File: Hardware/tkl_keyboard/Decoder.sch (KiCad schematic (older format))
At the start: 8 parts, among them U7 CD74HC238, U8 CD74HC238

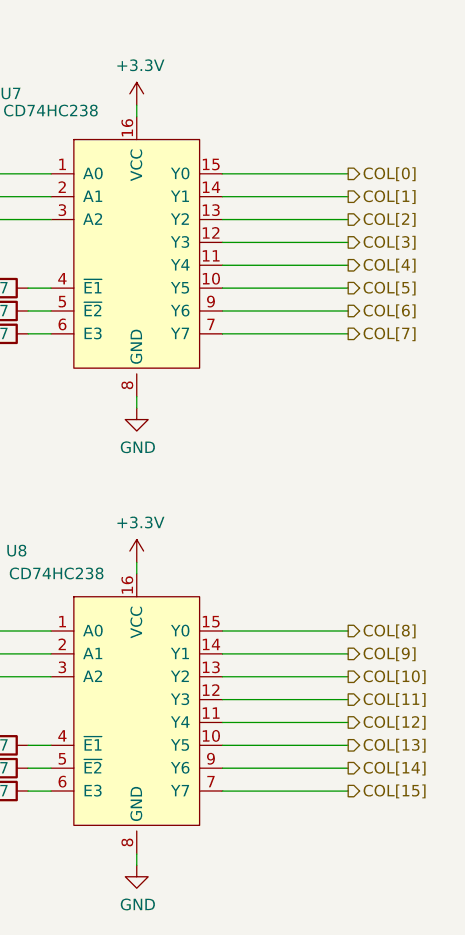
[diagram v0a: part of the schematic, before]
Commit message: LEDs and diodes routed
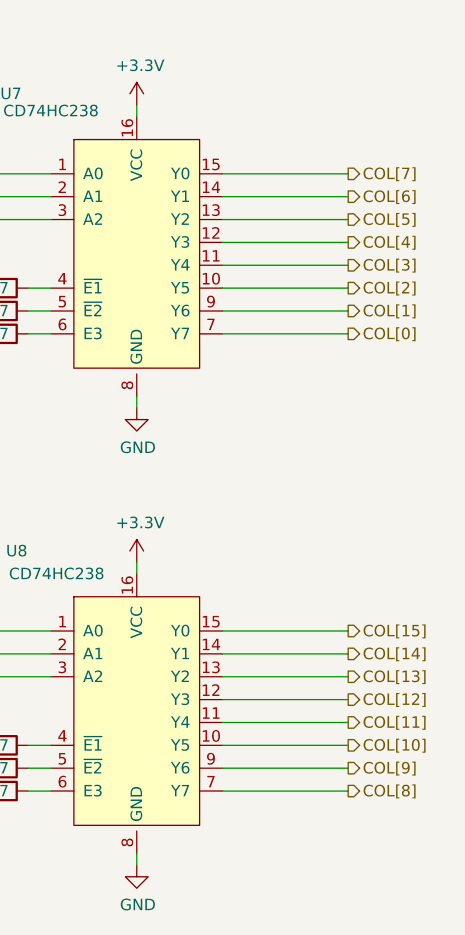
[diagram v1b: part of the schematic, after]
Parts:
- U7, U8: footprint (none) -> Package_SO:SOIC-16_3.9x9.9mm_P1.27mm
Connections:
- net COL[0]: now also U7.7 (Y7); no longer U7.15 (Y0)
- net COL[10]: now also U8.10 (Y5); no longer U8.13 (Y2)
- net COL[11]: now also U8.11 (Y4); no longer U8.12 (Y3)
- net COL[12]: now also U8.12 (Y3); no longer U8.11 (Y4)
- net COL[13]: now also U8.13 (Y2); no longer U8.10 (Y5)
- net COL[14]: now also U8.14 (Y1); no longer U8.9 (Y6)
- net COL[15]: now also U8.15 (Y0); no longer U8.7 (Y7)
- net COL[1]: now also U7.9 (Y6); no longer U7.14 (Y1)
- net COL[2]: now also U7.10 (Y5); no longer U7.13 (Y2)
- net COL[3]: now also U7.11 (Y4); no longer U7.12 (Y3)
- net COL[4]: now also U7.12 (Y3); no longer U7.11 (Y4)
- net COL[5]: now also U7.13 (Y2); no longer U7.10 (Y5)
- net COL[6]: now also U7.14 (Y1); no longer U7.9 (Y6)
- net COL[7]: now also U7.15 (Y0); no longer U7.7 (Y7)
- net COL[8]: now also U8.7 (Y7); no longer U8.15 (Y0)
- net COL[9]: now also U8.9 (Y6); no longer U8.14 (Y1)
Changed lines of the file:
@@
 F 0 "U7" H 5225 4700 50  0000 C CNN
 F 1 "CD74HC238" H 5400 4625 50  0000 C CNN
-F 2 "" H 5150 4600 50  0001 C CNN
+F 2 "Package_SO:SOIC-16_3.9x9.9mm_P1.27mm" H 5150 4600 50  0001 C CNN
 F 3 "" H 5150 4600 50  0001 C CNN
 	1    5775 3500
@@
 F 0 "U8" H 5250 6700 50  0000 C CNN
 F 1 "CD74HC238" H 5425 6600 50  0000 C CNN
-F 2 "" H 5150 6600 50  0001 C CNN
+F 2 "Package_SO:SOIC-16_3.9x9.9mm_P1.27mm" H 5150 6600 50  0001 C CNN
 F 3 "" H 5150 6600 50  0001 C CNN
 	1    5775 5500
@@
 Wire Wire Line
 	4850 4850 5400 4850
-Text HLabel 6700 2650 2    50   Output ~ 0
+Text HLabel 6700 3350 2    50   Output ~ 0
 COL[0]
 Wire Wire Line
-	6700 2650 6150 2650
-Text HLabel 6700 2750 2    50   Output ~ 0
+	6700 3350 6150 3350
+Text HLabel 6700 3250 2    50   Output ~ 0
 COL[1]
 Wire Wire Line
-	6700 2750 6150 2750
-Text HLabel 6700 2850 2    50   Output ~ 0
+	6700 3250 6150 3250
+Text HLabel 6700 3150 2    50   Output ~ 0
 COL[2]
 Wire Wire Line
-	6700 2850 6150 2850
-Text HLabel 6700 2950 2    50   Output ~ 0
+	6700 3150 6150 3150
+Text HLabel 6700 3050 2    50   Output ~ 0
 COL[3]
 Wire Wire Line
-	6700 2950 6150 2950
-Text HLabel 6700 3050 2    50   Output ~ 0
+	6700 3050 6150 3050
+Text HLabel 6700 2950 2    50   Output ~ 0
 COL[4]
 Wire Wire Line
-	6700 3050 6150 3050
-Text HLabel 6700 3150 2    50   Output ~ 0
+	6700 2950 6150 2950
+Text HLabel 6700 2850 2    50   Output ~ 0
 COL[5]
 Wire Wire Line
-	6700 3150 6150 3150
+	6700 2850 6150 2850
 Wire Wire Line
-	6700 3250 6150 3250
-Text HLabel 6700 3350 2    50   Output ~ 0
+	6700 2750 6150 2750
+Text HLabel 6700 2650 2    50   Output ~ 0
 COL[7]
 Wire Wire Line
-	6700 3350 6150 3350
-Text HLabel 6700 4650 2    50   Output ~ 0
+	6700 2650 6150 2650
+Text HLabel 6700 5350 2    50   Output ~ 0
 COL[8]
 Wire Wire Line
-	6700 4650 6150 4650
-Text HLabel 6700 4750 2    50   Output ~ 0
+	6700 5350 6150 5350
+Text HLabel 6700 5250 2    50   Output ~ 0
 COL[9]
 Wire Wire Line
-	6700 4750 6150 4750
-Text HLabel 6700 4850 2    50   Output ~ 0
+	6700 5250 6150 5250
+Text HLabel 6700 5150 2    50   Output ~ 0
 COL[10]
 Wire Wire Line
-	6700 4850 6150 4850
-Text HLabel 6700 4950 2    50   Output ~ 0
+	6700 5150 6150 5150
+Text HLabel 6700 5050 2    50   Output ~ 0
 COL[11]
 Wire Wire Line
-	6700 4950 6150 4950
-Text HLabel 6700 5050 2    50   Output ~ 0
+	6700 5050 6150 5050
+Text HLabel 6700 4950 2    50   Output ~ 0
 COL[12]
 Wire Wire Line
-	6700 5050 6150 5050
-Text HLabel 6700 5150 2    50   Output ~ 0
+	6700 4950 6150 4950
+Text HLabel 6700 4850 2    50   Output ~ 0
 COL[13]
 Wire Wire Line
-	6700 5150 6150 5150
-Text HLabel 6700 5250 2    50   Output ~ 0
+	6700 4850 6150 4850
+Text HLabel 6700 4750 2    50   Output ~ 0
 COL[14]
 Wire Wire Line
-	6700 5250 6150 5250
-Text HLabel 6700 5350 2    50   Output ~ 0
+	6700 4750 6150 4750
+Text HLabel 6700 4650 2    50   Output ~ 0
 COL[15]
 Wire Wire Line
-	6700 5350 6150 5350
-Text HLabel 6700 3250 2    50   Output ~ 0
+	6700 4650 6150 4650
+Text HLabel 6700 2750 2    50   Output ~ 0
 COL[6]
 $Comp

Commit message: Switch matrix routed
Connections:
- net COL[0]: now also U7.15 (Y0); no longer U7.7 (Y7)
- net COL[10]: now also U8.13 (Y2); no longer U8.10 (Y5)
- net COL[11]: now also U8.12 (Y3); no longer U8.11 (Y4)
- net COL[12]: now also U8.11 (Y4); no longer U8.12 (Y3)
- net COL[13]: now also U8.10 (Y5); no longer U8.13 (Y2)
- net COL[14]: now also U8.9 (Y6); no longer U8.14 (Y1)
- net COL[15]: now also U8.7 (Y7); no longer U8.15 (Y0)
- net COL[1]: now also U7.14 (Y1); no longer U7.9 (Y6)
- net COL[2]: now also U7.13 (Y2); no longer U7.10 (Y5)
- net COL[3]: now also U7.12 (Y3); no longer U7.11 (Y4)
- net COL[4]: now also U7.11 (Y4); no longer U7.12 (Y3)
- net COL[5]: now also U7.10 (Y5); no longer U7.13 (Y2)
- net COL[6]: now also U7.9 (Y6); no longer U7.14 (Y1)
- net COL[7]: now also U7.7 (Y7); no longer U7.15 (Y0)
- net COL[8]: now also U8.15 (Y0); no longer U8.7 (Y7)
- net COL[9]: now also U8.14 (Y1); no longer U8.9 (Y6)
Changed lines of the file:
@@
 Wire Wire Line
 	4850 4850 5400 4850
-Text HLabel 6700 3350 2    50   Output ~ 0
+Text HLabel 6700 2650 2    50   Output ~ 0
 COL[0]
 Wire Wire Line
-	6700 3350 6150 3350
-Text HLabel 6700 3250 2    50   Output ~ 0
+	6700 2650 6150 2650
+Text HLabel 6700 2750 2    50   Output ~ 0
 COL[1]
 Wire Wire Line
-	6700 3250 6150 3250
-Text HLabel 6700 3150 2    50   Output ~ 0
+	6700 2750 6150 2750
+Text HLabel 6700 2850 2    50   Output ~ 0
 COL[2]
 Wire Wire Line
-	6700 3150 6150 3150
-Text HLabel 6700 3050 2    50   Output ~ 0
+	6700 2850 6150 2850
+Text HLabel 6700 2950 2    50   Output ~ 0
 COL[3]
 Wire Wire Line
-	6700 3050 6150 3050
-Text HLabel 6700 2950 2    50   Output ~ 0
+	6700 2950 6150 2950
+Text HLabel 6700 3050 2    50   Output ~ 0
 COL[4]
 Wire Wire Line
-	6700 2950 6150 2950
-Text HLabel 6700 2850 2    50   Output ~ 0
+	6700 3050 6150 3050
+Text HLabel 6700 3150 2    50   Output ~ 0
 COL[5]
 Wire Wire Line
-	6700 2850 6150 2850
+	6700 3150 6150 3150
 Wire Wire Line
-	6700 2750 6150 2750
-Text HLabel 6700 2650 2    50   Output ~ 0
+	6700 3250 6150 3250
+Text HLabel 6700 3350 2    50   Output ~ 0
 COL[7]
 Wire Wire Line
-	6700 2650 6150 2650
-Text HLabel 6700 5350 2    50   Output ~ 0
+	6700 3350 6150 3350
+Text HLabel 6700 4650 2    50   Output ~ 0
 COL[8]
 Wire Wire Line
-	6700 5350 6150 5350
-Text HLabel 6700 5250 2    50   Output ~ 0
+	6700 4650 6150 4650
+Text HLabel 6700 4750 2    50   Output ~ 0
 COL[9]
 Wire Wire Line
-	6700 5250 6150 5250
-Text HLabel 6700 5150 2    50   Output ~ 0
+	6700 4750 6150 4750
+Text HLabel 6700 4850 2    50   Output ~ 0
 COL[10]
 Wire Wire Line
-	6700 5150 6150 5150
-Text HLabel 6700 5050 2    50   Output ~ 0
+	6700 4850 6150 4850
+Text HLabel 6700 4950 2    50   Output ~ 0
 COL[11]
 Wire Wire Line
-	6700 5050 6150 5050
-Text HLabel 6700 4950 2    50   Output ~ 0
+	6700 4950 6150 4950
+Text HLabel 6700 5050 2    50   Output ~ 0
 COL[12]
 Wire Wire Line
-	6700 4950 6150 4950
-Text HLabel 6700 4850 2    50   Output ~ 0
+	6700 5050 6150 5050
+Text HLabel 6700 5150 2    50   Output ~ 0
 COL[13]
 Wire Wire Line
-	6700 4850 6150 4850
-Text HLabel 6700 4750 2    50   Output ~ 0
+	6700 5150 6150 5150
+Text HLabel 6700 5250 2    50   Output ~ 0
 COL[14]
 Wire Wire Line
-	6700 4750 6150 4750
-Text HLabel 6700 4650 2    50   Output ~ 0
+	6700 5250 6150 5250
+Text HLabel 6700 5350 2    50   Output ~ 0
 COL[15]
 Wire Wire Line
-	6700 4650 6150 4650
-Text HLabel 6700 2750 2    50   Output ~ 0
+	6700 5350 6150 5350
+Text HLabel 6700 3250 2    50   Output ~ 0
 COL[6]
 $Comp

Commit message: Updating schematic
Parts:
- R24, R25, R26, R27, R28, R29: value 4K7 -> 10K
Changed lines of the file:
@@
 $Descr A4 11693 8268
 encoding utf-8
-Sheet 6 11
+Sheet 6 12
 Title ""
 Date ""
@@
 AR Path="/6301FD9D/631288D4" Ref="R24"  Part="1"
 F 0 "R24" V 5150 2750 50  0000 C CNN
-F 1 "4K7" V 5150 3150 50  0000 C CNN
+F 1 "10K" V 5150 3150 50  0000 C CNN
 F 2 "resistor_smd:R_0603_1608Metric" V 5080 3150 50  0001 C CNN
 F 3 "~" H 5150 3150 50  0001 C CNN
@@
 AR Path="/6301FD9D/63128CD2" Ref="R25"  Part="1"
 F 0 "R25" V 5150 2850 50  0000 C CNN
-F 1 "4K7" V 5150 3250 50  0000 C CNN
+F 1 "10K" V 5150 3250 50  0000 C CNN
 F 2 "resistor_smd:R_0603_1608Metric" V 5080 3250 50  0001 C CNN
 F 3 "~" H 5150 3250 50  0001 C CNN
@@
 AR Path="/6301FD9D/63129160" Ref="R26"  Part="1"
 F 0 "R26" V 5150 2950 50  0000 C CNN
-F 1 "4K7" V 5150 3350 50  0000 C CNN
+F 1 "10K" V 5150 3350 50  0000 C CNN
 F 2 "resistor_smd:R_0603_1608Metric" V 5080 3350 50  0001 C CNN
 F 3 "~" H 5150 3350 50  0001 C CNN
@@
 AR Path="/6301FD9D/63130BA6" Ref="R27"  Part="1"
 F 0 "R27" V 5150 4750 50  0000 C CNN
-F 1 "4K7" V 5150 5150 50  0000 C CNN
+F 1 "10K" V 5150 5150 50  0000 C CNN
 F 2 "resistor_smd:R_0603_1608Metric" V 5080 5150 50  0001 C CNN
 F 3 "~" H 5150 5150 50  0001 C CNN
@@
 AR Path="/6301FD9D/63130BAC" Ref="R28"  Part="1"
 F 0 "R28" V 5150 4850 50  0000 C CNN
-F 1 "4K7" V 5150 5250 50  0000 C CNN
+F 1 "10K" V 5150 5250 50  0000 C CNN
 F 2 "resistor_smd:R_0603_1608Metric" V 5080 5250 50  0001 C CNN
 F 3 "~" H 5150 5250 50  0001 C CNN
@@
 AR Path="/6301FD9D/63130BB2" Ref="R29"  Part="1"
 F 0 "R29" V 5150 4950 50  0000 C CNN
-F 1 "4K7" V 5150 5350 50  0000 C CNN
+F 1 "10K" V 5150 5350 50  0000 C CNN
 F 2 "resistor_smd:R_0603_1608Metric" V 5080 5350 50  0001 C CNN
 F 3 "~" H 5150 5350 50  0001 C CNN

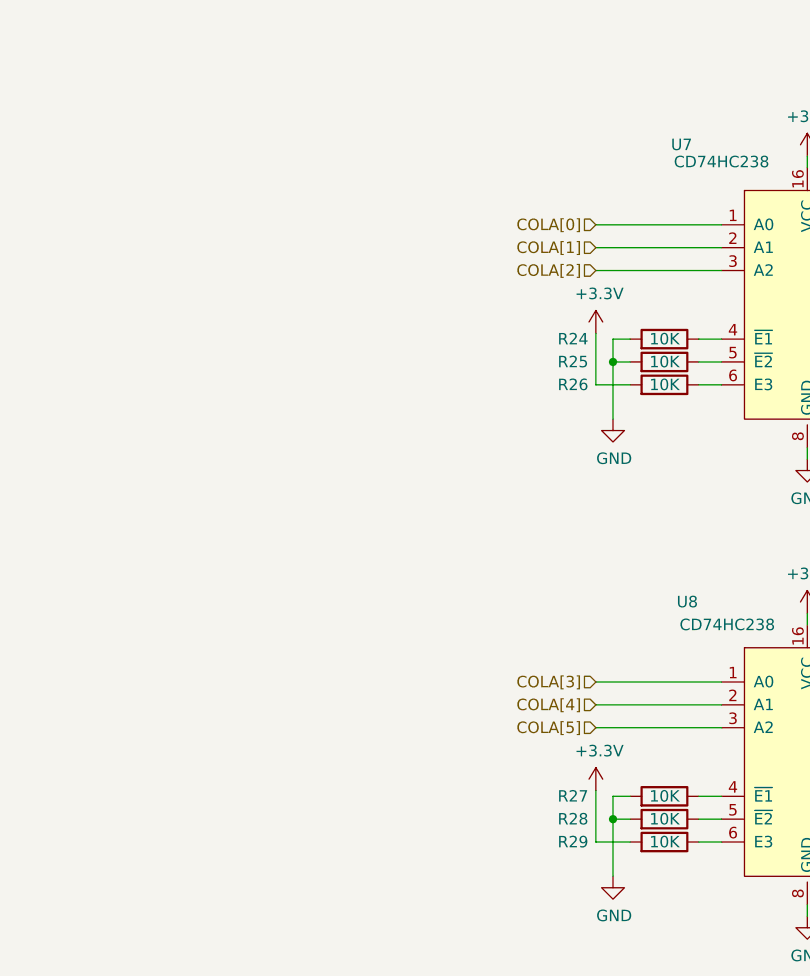
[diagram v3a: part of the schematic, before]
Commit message: Added some missing capacitors, Fixed DC jack footprint connections
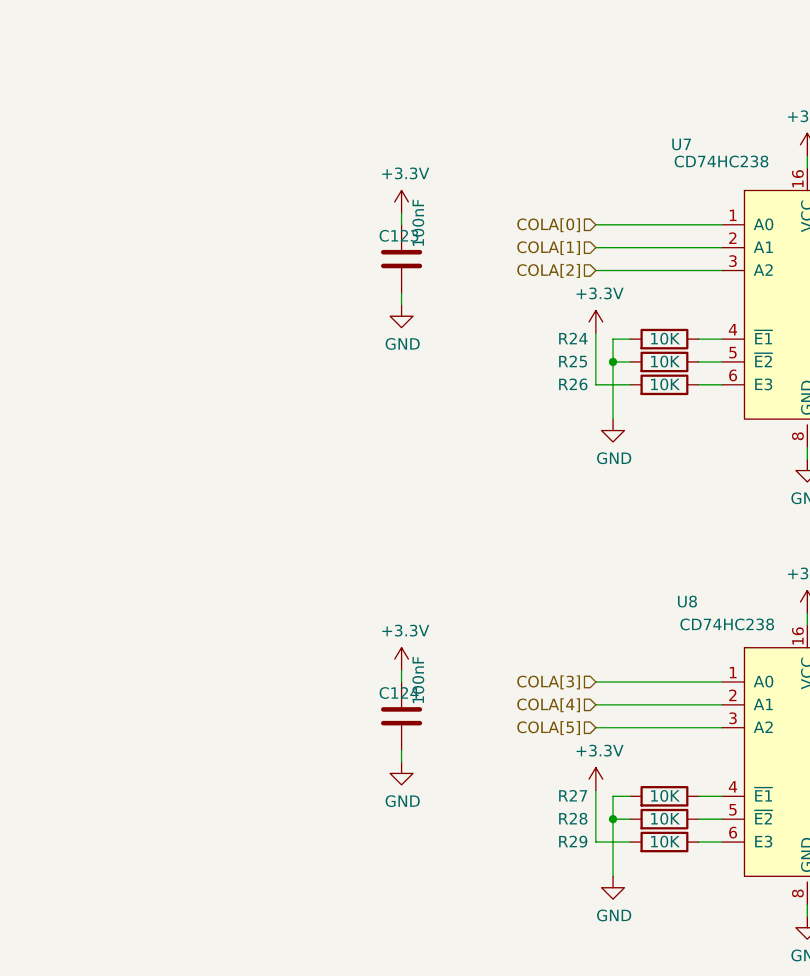
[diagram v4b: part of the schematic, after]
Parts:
- added C123, C124: 100nF, Capacitor_smd:C_0603_1608Metric, symbol Device:C
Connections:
- net +3V3: now also C123.1, C124.1
- net GND: now also C123.2, C124.2
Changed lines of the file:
@@
 Wire Wire Line
 	4850 5350 5000 5350
+Wire Wire Line
+	4000 2650 4000 2600
+Wire Wire Line
+	4000 2950 4000 3000
+$Comp
+L power:GND #PWR?
+U 1 1 616D26BD
+P 4000 3000
+AR Path="/616D26BD" Ref="#PWR?"  Part="1"
+AR Path="/60D44BDB/616D26BD" Ref="#PWR?"  Part="1"
+AR Path="/60D99CF5/616D26BD" Ref="#PWR?"  Part="1"
+AR Path="/60D44364/616D26BD" Ref="#PWR?"  Part="1"
+AR Path="/61150193/616D26BD" Ref="#PWR?"  Part="1"
+AR Path="/61D5AB4C/616D26BD" Ref="#PWR?"  Part="1"
+AR Path="/61234213/616D26BD" Ref="#PWR?"  Part="1"
+AR Path="/62FB59AD/616D26BD" Ref="#PWR?"  Part="1"
+AR Path="/6301FD9D/616D26BD" Ref="#PWR0523"  Part="1"
+F 0 "#PWR0523" H 4000 2750 50  0001 C CNN
+F 1 "GND" H 4005 2827 50  0000 C CNN
+F 2 "" H 4000 3000 50  0001 C CNN
+F 3 "" H 4000 3000 50  0001 C CNN
+	1    4000 3000
+	1    0    0    -1
+$EndComp
+$Comp
+L Device:C C?
+U 1 1 616D26C3
+P 4000 2800
+AR Path="/616D26C3" Ref="C?"  Part="1"
+AR Path="/60D44BDB/616D26C3" Ref="C?"  Part="1"
+AR Path="/60D99CF5/616D26C3" Ref="C?"  Part="1"
+AR Path="/60D44364/616D26C3" Ref="C?"  Part="1"
+AR Path="/61150193/616D26C3" Ref="C?"  Part="1"
+AR Path="/61D5AB4C/616D26C3" Ref="C?"  Part="1"
+AR Path="/61234213/616D26C3" Ref="C?"  Part="1"
+AR Path="/62FB59AD/616D26C3" Ref="C?"  Part="1"
+AR Path="/6301FD9D/616D26C3" Ref="C123"  Part="1"
+F 0 "C123" H 3900 2900 50  0000 L CNN
+F 1 "100nF" V 4075 2850 50  0000 L CNN
+F 2 "Capacitor_smd:C_0603_1608Metric" H 4038 2650 50  0001 C CNN
+F 3 "~" H 4000 2800 50  0001 C CNN
+	1    4000 2800
+	1    0    0    -1
+$EndComp
+$Comp
+L power:+3.3V #PWR?
+U 1 1 616D3E4D
+P 4000 2600
+AR Path="/616D3E4D" Ref="#PWR?"  Part="1"
+AR Path="/60D44BDB/616D3E4D" Ref="#PWR?"  Part="1"
+AR Path="/60D99CF5/616D3E4D" Ref="#PWR?"  Part="1"
+AR Path="/6114D32E/616D3E4D" Ref="#PWR?"  Part="1"
+AR Path="/6247A5CE/616D3E4D" Ref="#PWR?"  Part="1"
+AR Path="/612340DE/616D3E4D" Ref="#PWR?"  Part="1"
+AR Path="/62F6B81F/616D3E4D" Ref="#PWR?"  Part="1"
+AR Path="/6301FD9D/616D3E4D" Ref="#PWR0531"  Part="1"
+F 0 "#PWR0531" H 4000 2450 50  0001 C CNN
+F 1 "+3.3V" H 4015 2773 50  0000 C CNN
+F 2 "" H 4000 2600 50  0001 C CNN
+F 3 "" H 4000 2600 50  0001 C CNN
+	1    4000 2600
+	1    0    0    -1
+$EndComp
+Wire Wire Line
+	4000 4950 4000 5000
+$Comp
+L power:GND #PWR?
+U 1 1 616D9D88
+P 4000 5000
+AR Path="/616D9D88" Ref="#PWR?"  Part="1"
+AR Path="/60D44BDB/616D9D88" Ref="#PWR?"  Part="1"
+AR Path="/60D99CF5/616D9D88" Ref="#PWR?"  Part="1"
+AR Path="/60D44364/616D9D88" Ref="#PWR?"  Part="1"
+AR Path="/61150193/616D9D88" Ref="#PWR?"  Part="1"
+AR Path="/61D5AB4C/616D9D88" Ref="#PWR?"  Part="1"
+AR Path="/61234213/616D9D88" Ref="#PWR?"  Part="1"
+AR Path="/62FB59AD/616D9D88" Ref="#PWR?"  Part="1"
+AR Path="/6301FD9D/616D9D88" Ref="#PWR0532"  Part="1"
+F 0 "#PWR0532" H 4000 4750 50  0001 C CNN
+F 1 "GND" H 4005 4827 50  0000 C CNN
+F 2 "" H 4000 5000 50  0001 C CNN
+F 3 "" H 4000 5000 50  0001 C CNN
+	1    4000 5000
+	1    0    0    -1
+$EndComp
+$Comp
+L Device:C C?
+U 1 1 616D9D8E
+P 4000 4800
+AR Path="/616D9D8E" Ref="C?"  Part="1"
+AR Path="/60D44BDB/616D9D8E" Ref="C?"  Part="1"
+AR Path="/60D99CF5/616D9D8E" Ref="C?"  Part="1"
+AR Path="/60D44364/616D9D8E" Ref="C?"  Part="1"
+AR Path="/61150193/616D9D8E" Ref="C?"  Part="1"
+AR Path="/61D5AB4C/616D9D8E" Ref="C?"  Part="1"
+AR Path="/61234213/616D9D8E" Ref="C?"  Part="1"
+AR Path="/62FB59AD/616D9D8E" Ref="C?"  Part="1"
+AR Path="/6301FD9D/616D9D8E" Ref="C124"  Part="1"
+F 0 "C124" H 3900 4900 50  0000 L CNN
+F 1 "100nF" V 4075 4850 50  0000 L CNN
+F 2 "Capacitor_smd:C_0603_1608Metric" H 4038 4650 50  0001 C CNN
+F 3 "~" H 4000 4800 50  0001 C CNN
+	1    4000 4800
+	1    0    0    -1
+$EndComp
+Wire Wire Line
+	4000 4650 4000 4600
+$Comp
+L power:+3.3V #PWR?
+U 1 1 616DBFA1
+P 4000 4600
+AR Path="/616DBFA1" Ref="#PWR?"  Part="1"
+AR Path="/60D44BDB/616DBFA1" Ref="#PWR?"  Part="1"
+AR Path="/60D99CF5/616DBFA1" Ref="#PWR?"  Part="1"
+AR Path="/6114D32E/616DBFA1" Ref="#PWR?"  Part="1"
+AR Path="/6247A5CE/616DBFA1" Ref="#PWR?"  Part="1"
+AR Path="/612340DE/616DBFA1" Ref="#PWR?"  Part="1"
+AR Path="/62F6B81F/616DBFA1" Ref="#PWR?"  Part="1"
+AR Path="/6301FD9D/616DBFA1" Ref="#PWR0533"  Part="1"
+F 0 "#PWR0533" H 4000 4450 50  0001 C CNN
+F 1 "+3.3V" H 4015 4773 50  0000 C CNN
+F 2 "" H 4000 4600 50  0001 C CNN
+F 3 "" H 4000 4600 50  0001 C CNN
+	1    4000 4600
+	1    0    0    -1
+$EndComp
 $EndSCHEMATC
